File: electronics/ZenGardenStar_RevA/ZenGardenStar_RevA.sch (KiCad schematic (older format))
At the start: 20 parts, among them P1 CONN_01X02, P2 CONN_01X02, U1 A6211, U2 LM317_SOT223, U3 ArduinoProMini328, U4 MCP1700, U5 NRF24L01+

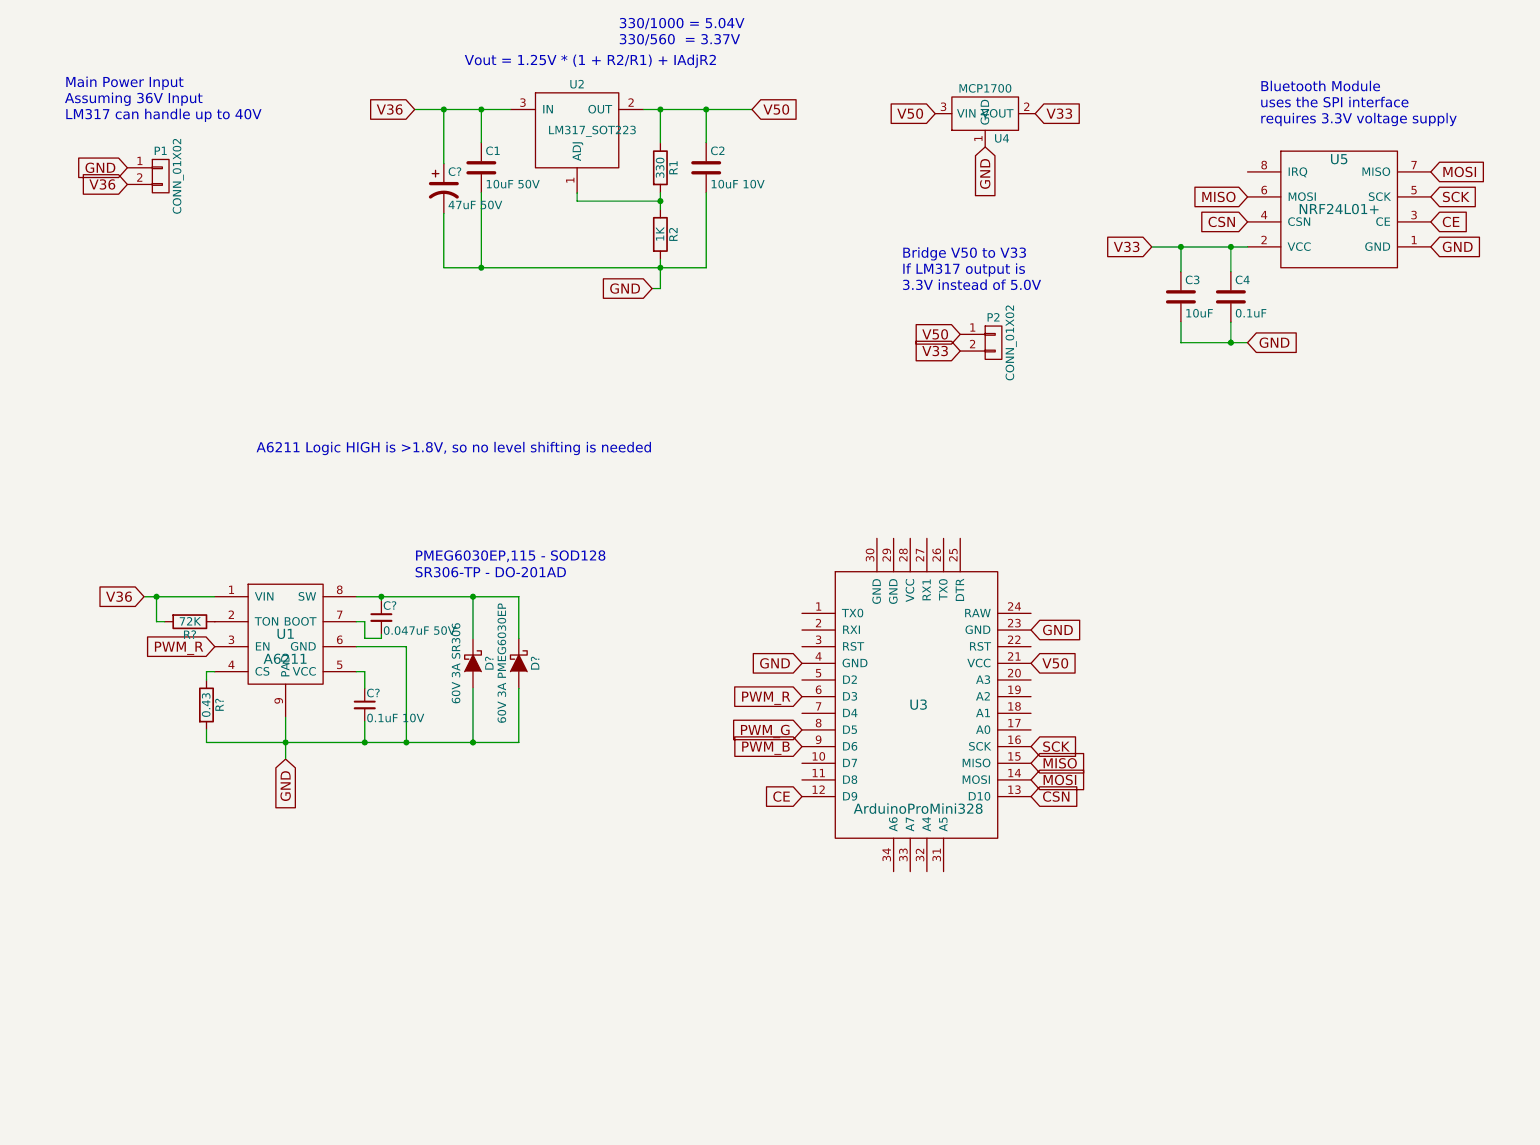
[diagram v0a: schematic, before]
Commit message: updated schematic for star
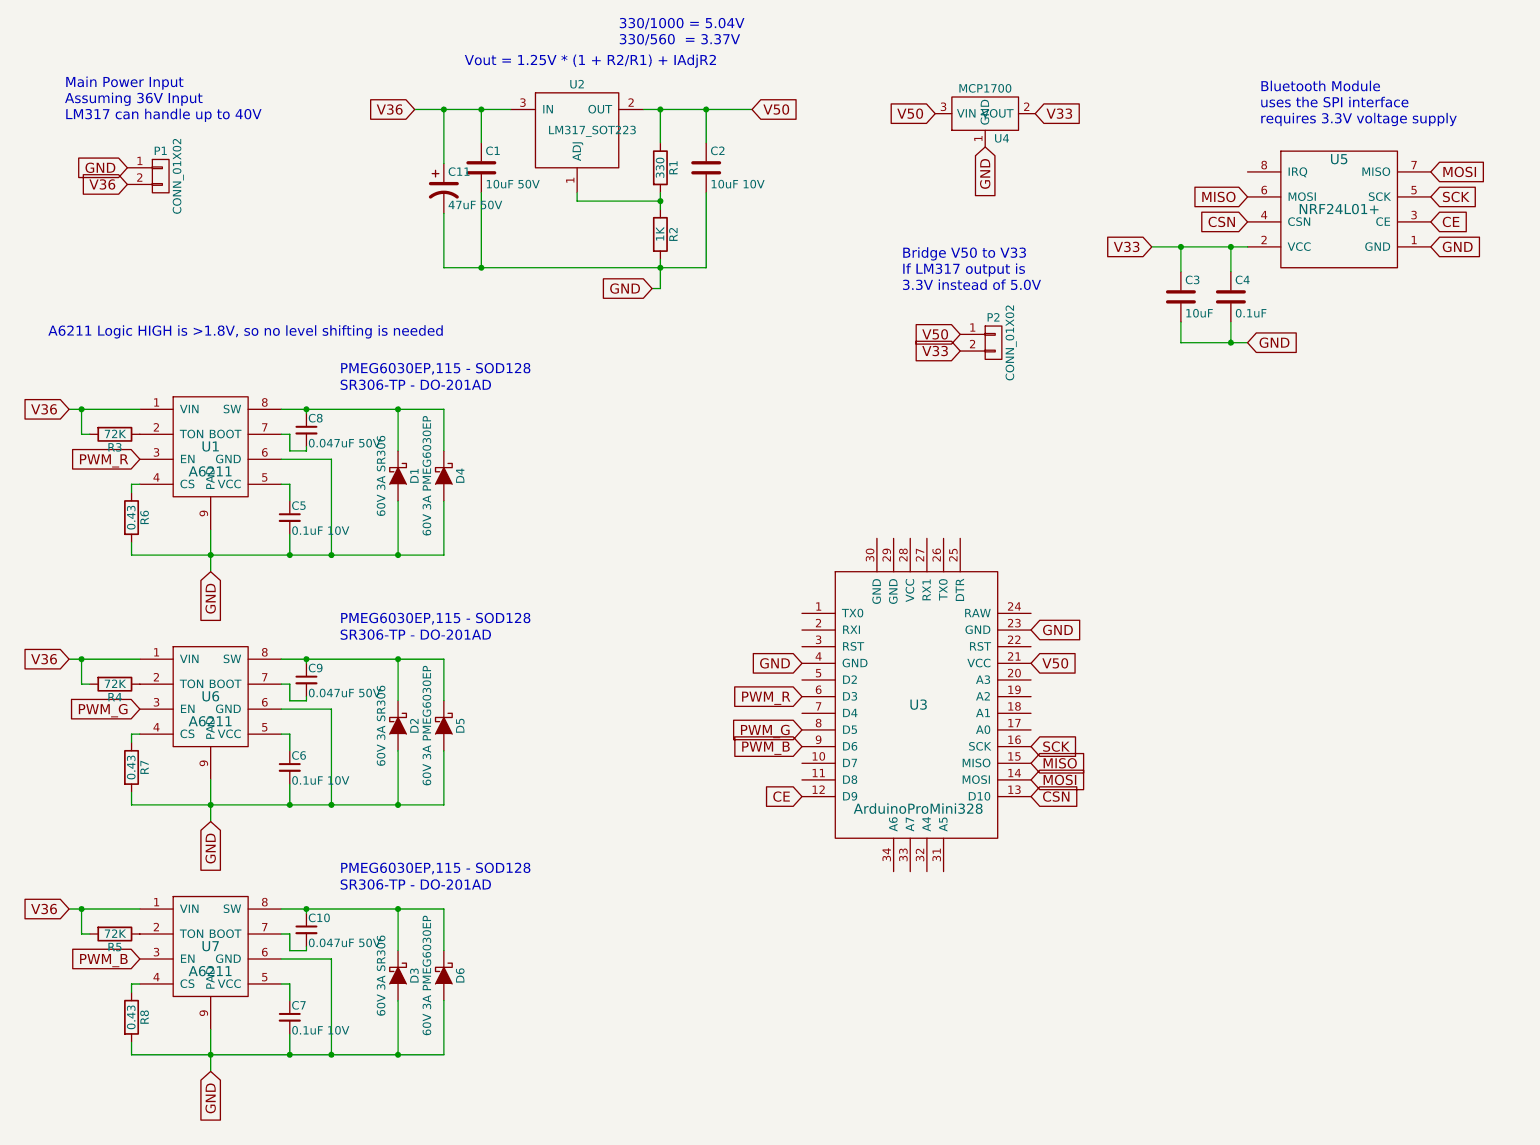
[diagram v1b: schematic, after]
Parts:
- added C10, C9: 0.047uF 50V, Capacitors_SMD:C_0805, symbol C_Small
- added C6, C7: 0.1uF 10V, Capacitors_SMD:C_0805, symbol C_Small
- added D2, D3: 60V 3A SR306, Diodes_ThroughHole:Diode_DO-201AD_Horizontal_RM15, symbol D_Schottky
- added D5, D6: 60V 3A PMEG6030EP, Diodes_SMD:SOD-123, symbol D_Schottky
- added R4, R5: 72K, Resistors_SMD:R_1206, symbol R
- added R7, R8: 0.43, Resistors_SMD:R_1206, symbol R
- added U6, U7: A6211, Housings_SOIC:SOIC-8-1EP_3.9x4.9mm_Pitch1.27mm, symbol A6211
- C11: renamed from C?; footprint (none) -> Capacitors_ThroughHole:C_Radial_D7.5_L11.2_P2.5
- C5, C8: renamed from C?; footprint (none) -> Capacitors_SMD:C_0805
- D1: renamed from D?; footprint (none) -> Diodes_ThroughHole:Diode_DO-201AD_Horizontal_RM15
- D4: renamed from D?; footprint (none) -> Diodes_SMD:SOD-123
- gave numbers to parts that had none: 2
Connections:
- net GND: now also C6.2, C7.2, D2.2 (A), D3.2 (A), D5.2 (A), D6.2 (A), R7.2, R8.2, U6.6 (GND), U6.9 (PAD), U7.6 (GND), U7.9 (PAD)
- net PWM_B: now also U7.3 (EN)
- net PWM_G: now also U6.3 (EN)
- net V36: now also R4.2, R5.2, U6.1 (VIN), U7.1 (VIN)
- new net: R4.1, U6.2 (TON)
- new net: R7.1, U6.4 (CS)
- new net: C6.1, U6.5 (VCC)
- new net: C9.2, U6.7 (BOOT)
- new net: C9.1, D2.1 (K), D5.1 (K), U6.8 (SW)
- new net: R5.1, U7.2 (TON)
- new net: R8.1, U7.4 (CS)
- new net: C7.1, U7.5 (VCC)
- new net: C10.2, U7.7 (BOOT)
- new net: C10.1, D3.1 (K), D6.1 (K), U7.8 (SW)
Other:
- moved on the sheet: C5, C8, D1, D4, R3, R6, U1

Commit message: updated star layout and schematic and render, at 80-90% done
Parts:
- added L1, L2, L3: INDUCTOR_SMALL, Inductors:SELF-WE-PD-XXL, symbol INDUCTOR_SMALL
- added P3: CONN_PIR_0, Pin_Headers:Pin_Header_Straight_1x03, symbol CONN_01X03
- added P4: CONN_PIR_1, Pin_Headers:Pin_Header_Straight_1x03, symbol CONN_01X03
- added P5: CONN_R, Pin_Headers:Pin_Header_Straight_1x02, symbol CONN_01X02
- added P6: CONN_B, Pin_Headers:Pin_Header_Straight_1x02, symbol CONN_01X02
- added P7: CONN_G, Pin_Headers:Pin_Header_Straight_1x02, symbol CONN_01X02
- P2: value CONN_01X02 -> CONN_VDD
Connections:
- net GND: now also P3.1 (P1), P4.1 (P1)
- net V50: now also P3.3 (P3), P4.3 (P3)
- net PIR_0: now reaches U3.10 (D7)
- net PIR_0: now also P3.2 (P2)
- net PIR_1: now reaches U3.11 (D8)
- net PIR_1: now also P4.2 (P2)
- net at R6.1, U1.4 (CS): now also P5.1 (P1)
- net at C8.1, D1.1 (K), D4.1 (K)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: now also L1.1
- net at R7.1, U6.4 (CS): now also P7.1 (P1)
- net at C9.1, D2.1 (K), D5.1 (K)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: now also L2.1
- net at R8.1, U7.4 (CS): now also P6.1 (P1)
- net at C10.1, D3.1 (K), D6.1 (K)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: now also L3.1
- new net: L1.2, P5.2 (P2)
- new net: L2.2, P7.2 (P2)
- new net: L3.2, P6.2 (P2)
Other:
- note added: "PIR Sensor 5-20V Input\n3.3V Digital Output"
- moved on the sheet: R6, R7, R8

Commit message: some updates to the star schematics and layout; schematic pretty much final
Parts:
- added C12: 100uF 50V, Capacitors_ThroughHole:C_Radial_D8_L13_P3.8, symbol CP1
- added P10: CONN_I2C, Pin_Headers:Pin_Header_Straight_1x04, symbol CONN_01X04
- added P8: CONN_A0, Pin_Headers:Pin_Header_Straight_1x03, symbol CONN_01X03
- added P9: CONN_A1, Pin_Headers:Pin_Header_Straight_1x03, symbol CONN_01X03
- L1, L2, L3: value INDUCTOR_SMALL -> 47uH 1A; footprint Inductors:SELF-WE-PD-XXL -> MyKiCadParts:TAIYO_YUDEN_IND_6045
- P1: footprint Terminal_Blocks:TerminalBlock_Pheonix_PT-3.5mm_2pol -> Connect:AK300-2
- P3, P4: footprint Pin_Headers:Pin_Header_Straight_1x03 -> Pin_Headers:Pin_Header_Angled_1x03
- P5, P6, P7: footprint Pin_Headers:Pin_Header_Straight_1x02 -> Connect:AK300-2
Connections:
- net GND: now also C12.2, P10.1 (P1), P8.1 (P1), P9.1 (P1)
- net V36: now also C12.1
- net V50: now also P10.2 (P2), P8.2 (P2), P9.2 (P2)
- net A0: now reaches U3.17 (A0)
- net A0: now also P8.3 (P3)
- net A1: now reaches U3.18 (A1)
- net A1: now also P9.3 (P3)
- net SCL: now reaches U3.31 (A5)
- net SCL: now also P10.4 (P4)
- net SDA: now reaches U3.32 (A4)
- net SDA: now also P10.3 (P3)
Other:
- note added: "Bluetooth Module\nuses the SPI interface\nrequires 3.3V voltage supply\npins are 5V tolerant though"
- note added: "PMEG6030EP,115 - SOD128 OR"
- note removed: "Bluetooth Module\nuses the SPI interface\nrequires 3.3V voltage supply"
- moved on the sheet: P3, P4, U3
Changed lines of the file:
@@
 Sheet 1 1
 Title "ZenGardenStar"
-Date "2017-03-09"
+Date "2017-03-11"
 Rev "A"
 Comp "D.O.P.E."
@@
 F 0 "P1" H 1925 2000 50  0000 C CNN
 F 1 "CONN_01X02" V 2025 1850 50  0000 C CNN
-F 2 "Terminal_Blocks:TerminalBlock_Pheonix_PT-3.5mm_2pol" H 1925 1850 50  0001 C CNN
+F 2 "Connect:AK300-2" H 1925 1850 50  0001 C CNN
 F 3 "" H 1925 1850 50  0000 C CNN
 	1    1925 1850
@@
 L ArduinoProMini328 U3
 U 1 1 58BB7402
-P 6475 5025
-F 0 "U3" H 6475 5025 60  0000 C CNN
-F 1 "ArduinoProMini328" H 6475 4400 60  0000 C CNN
-F 2 "MyKiCadParts:ArduinoProMini328" H 6475 5025 60  0001 C CNN
-F 3 "" H 6475 5025 60  0001 C CNN
-	1    6475 5025
+P 6550 4750
+F 0 "U3" H 6550 4750 60  0000 C CNN
+F 1 "ArduinoProMini328" H 6550 4125 60  0000 C CNN
+F 2 "MyKiCadParts:ArduinoProMini328" H 6550 4750 60  0001 C CNN
+F 3 "" H 6550 4750 60  0001 C CNN
+	1    6550 4750
 	1    0    0    -1
 $EndComp
 Text GLabel 7875 2275 0    60   Input ~ 0
 V33
-Text GLabel 7150 5275 2    60   Input ~ 0
+Text GLabel 7225 5000 2    60   Input ~ 0
 SCK
-Text GLabel 7150 5375 2    60   Input ~ 0
+Text GLabel 7225 5100 2    60   Input ~ 0
 MISO
-Text GLabel 7150 5475 2    60   Input ~ 0
+Text GLabel 7225 5200 2    60   Input ~ 0
 MOSI
-Text GLabel 7150 5575 2    60   Input ~ 0
+Text GLabel 7225 5300 2    60   Input ~ 0
 CSN
-Text GLabel 5775 5575 0    60   Input ~ 0
+Text GLabel 5850 5300 0    60   Input ~ 0
 CE
 Text GLabel 9550 2125 2    60   Input ~ 0
@@
 Text GLabel 9550 1825 2    60   Input ~ 0
 MOSI
-Text GLabel 7150 4575 2    60   Input ~ 0
+Text GLabel 7225 4300 2    60   Input ~ 0
 GND
 Text GLabel 9550 2275 2    60   Input ~ 0
@@
 GND
 Text Notes 8525 1550 0    60   ~ 0
-Bluetooth Module\nuses the SPI interface\nrequires 3.3V voltage supply
-Text GLabel 5775 4975 0    60   Input ~ 0
+Bluetooth Module\nuses the SPI interface\nrequires 3.3V voltage supply\npins are 5V tolerant though
+Text GLabel 5850 4700 0    60   Input ~ 0
 PWM_R
-Text GLabel 5775 5175 0    60   Input ~ 0
+Text GLabel 5850 4900 0    60   Input ~ 0
 PWM_G
-Text GLabel 5775 5275 0    60   Input ~ 0
+Text GLabel 5850 5000 0    60   Input ~ 0
 PWM_B
-Text GLabel 5775 4775 0    60   Input ~ 0
-GND
-Text GLabel 7150 4775 2    60   Input ~ 0
+Text GLabel 5850 4500 0    60   Input ~ 0
+GND
+Text GLabel 7225 4500 2    60   Input ~ 0
 V50
 Text GLabel 6575 1475 0    60   Input ~ 0
@@
 	1    0    0    -1
 $EndComp
-Text GLabel 3450 1450 0    60   Input ~ 0
+Text GLabel 3075 1450 0    60   Input ~ 0
 V36
 Text GLabel 4875 2525 0    60   Input ~ 0
@@
 $EndComp
 Text Notes 3000 3050 0    60   ~ 0
-PMEG6030EP,115 - SOD128
+PMEG6030EP,115 - SOD128   OR
 Text Notes 3000 3150 0    60   ~ 0
 SR306-TP - DO-201AD
@@
 L CONN_01X03 P3
 U 1 1 58C21485
-P 8550 4550
-F 0 "P3" H 8550 4750 50  0000 C CNN
-F 1 "CONN_PIR_0" V 8650 4550 50  0000 C CNN
-F 2 "Pin_Headers:Pin_Header_Straight_1x03" H 8550 4550 50  0001 C CNN
-F 3 "" H 8550 4550 50  0000 C CNN
-	1    8550 4550
-	1    0    0    -1
-$EndComp
-Text GLabel 8350 4650 0    60   Input ~ 0
+P 8950 4075
+F 0 "P3" H 8950 4275 50  0000 C CNN
+F 1 "CONN_PIR_0" V 9050 4075 50  0000 C CNN
+F 2 "Pin_Headers:Pin_Header_Angled_1x03" H 8950 4075 50  0001 C CNN
+F 3 "" H 8950 4075 50  0000 C CNN
+	1    8950 4075
+	1    0    0    -1
+$EndComp
+Text GLabel 8750 4175 0    60   Input ~ 0
 V50
-Text GLabel 8350 4450 0    60   Input ~ 0
-GND
-Text GLabel 8350 4550 0    60   Input ~ 0
+Text GLabel 8750 3975 0    60   Input ~ 0
+GND
+Text GLabel 8750 4075 0    60   Input ~ 0
 PIR_0
-Text GLabel 5775 5375 0    60   Input ~ 0
+Text GLabel 5850 5100 0    60   Input ~ 0
 PIR_0
-Text GLabel 5775 5475 0    60   Input ~ 0
+Text GLabel 5850 5200 0    60   Input ~ 0
 PIR_1
 $Comp
 L CONN_01X03 P4
 U 1 1 58C22968
-P 8550 5125
-F 0 "P4" H 8550 5325 50  0000 C CNN
-F 1 "CONN_PIR_1" V 8650 5125 50  0000 C CNN
-F 2 "Pin_Headers:Pin_Header_Straight_1x03" H 8550 5125 50  0001 C CNN
-F 3 "" H 8550 5125 50  0000 C CNN
-	1    8550 5125
-	1    0    0    -1
-$EndComp
-Text GLabel 8350 5225 0    60   Input ~ 0
+P 8950 4650
+F 0 "P4" H 8950 4850 50  0000 C CNN
+F 1 "CONN_PIR_1" V 9050 4650 50  0000 C CNN
+F 2 "Pin_Headers:Pin_Header_Angled_1x03" H 8950 4650 50  0001 C CNN
+F 3 "" H 8950 4650 50  0000 C CNN
+	1    8950 4650
+	1    0    0    -1
+$EndComp
+Text GLabel 8750 4750 0    60   Input ~ 0
 V50
-Text GLabel 8350 5025 0    60   Input ~ 0
-GND
-Text GLabel 8350 5125 0    60   Input ~ 0
+Text GLabel 8750 4550 0    60   Input ~ 0
+GND
+Text GLabel 8750 4650 0    60   Input ~ 0
 PIR_1
-Text Notes 7925 4200 0    60   ~ 0
+Text Notes 8325 3725 0    60   ~ 0
 PIR Sensor 5-20V Input\n3.3V Digital Output
 $Comp
@@
 F 0 "P7" H 4525 5150 50  0000 C CNN
 F 1 "CONN_G" V 4625 5000 50  0000 C CNN
-F 2 "Pin_Headers:Pin_Header_Straight_1x02" H 4525 5000 50  0001 C CNN
+F 2 "Connect:AK300-2" H 4525 5000 50  0001 C CNN
 F 3 "" H 4525 5000 50  0000 C CNN
 	1    4525 5000
@@
 F 0 "P6" H 4500 6650 50  0000 C CNN
 F 1 "CONN_B" V 4600 6500 50  0000 C CNN
-F 2 "Pin_Headers:Pin_Header_Straight_1x02" H 4500 6500 50  0001 C CNN
+F 2 "Connect:AK300-2" H 4500 6500 50  0001 C CNN
 F 3 "" H 4500 6500 50  0000 C CNN
 	1    4500 6500
@@
 P 3925 3250
 F 0 "L1" H 3925 3350 50  0000 C CNN
-F 1 "INDUCTOR_SMALL" H 3925 3200 50  0000 C CNN
-F 2 "Inductors:SELF-WE-PD-XXL" H 3925 3250 50  0001 C CNN
+F 1 "47uH 1A" H 3925 3200 50  0000 C CNN
+F 2 "MyKiCadParts:TAIYO_YUDEN_IND_6045" H 3925 3250 50  0001 C CNN
 F 3 "" H 3925 3250 50  0000 C CNN
 	1    3925 3250
@@
 P 3925 4750
 F 0 "L2" H 3925 4850 50  0000 C CNN
-F 1 "INDUCTOR_SMALL" H 3925 4700 50  0000 C CNN
-F 2 "Inductors:SELF-WE-PD-XXL" H 3925 4750 50  0001 C CNN
+F 1 "47uH 1A" H 3925 4700 50  0000 C CNN
+F 2 "MyKiCadParts:TAIYO_YUDEN_IND_6045" H 3925 4750 50  0001 C CNN
 F 3 "" H 3925 4750 50  0000 C CNN
 	1    3925 4750
@@
 P 3925 6250
 F 0 "L3" H 3925 6350 50  0000 C CNN
-F 1 "INDUCTOR_SMALL" H 3925 6200 50  0000 C CNN
-F 2 "Inductors:SELF-WE-PD-XXL" H 3925 6250 50  0001 C CNN
+F 1 "47uH 1A" H 3925 6200 50  0000 C CNN
+F 2 "MyKiCadParts:TAIYO_YUDEN_IND_6045" H 3925 6250 50  0001 C CNN
 F 3 "" H 3925 6250 50  0000 C CNN
 	1    3925 6250
@@
 	4925 2350 4925 2525
 Wire Wire Line
-	3450 1450 4025 1450
+	3075 1450 4025 1450
 Wire Wire Line
 	4825 1450 5475 1450
@@
 	5200 2400 5200 1950
 Wire Wire Line
-	3625 2400 5200 2400
+	3325 2400 5200 2400
 Wire Wire Line
 	3850 2400 3850 1950
@@
 F 0 "P5" H 4475 3650 50  0000 C CNN
 F 1 "CONN_R" V 4575 3500 50  0000 C CNN
-F 2 "Pin_Headers:Pin_Header_Straight_1x02" H 4475 3500 50  0001 C CNN
+F 2 "Connect:AK300-2" H 4475 3500 50  0001 C CNN
 F 3 "" H 4475 3500 50  0000 C CNN
 	1    4475 3500
@@
 	3950 5250 3950 5050
 Connection ~ 4225 5050
+$Comp
+L CP1 C12
+U 1 1 58C46F27
+P 3325 2075
+F 0 "C12" H 3350 2175 50  0000 L CNN
+F 1 "100uF 50V" H 3350 1975 50  0000 L CNN
+F 2 "Capacitors_ThroughHole:C_Radial_D8_L13_P3.8" H 3325 2075 50  0001 C CNN
+F 3 "" H 3325 2075 50  0000 C CNN
+	1    3325 2075
+	1    0    0    -1
+$EndComp
+Wire Wire Line
+	3325 1925 3325 1450
+Connection ~ 3325 1450
+Wire Wire Line
+	3325 2225 3325 2400
+Connection ~ 3625 2400
+$Comp
+L CONN_01X03 P8
+U 1 1 58C4CE75
+P 8975 5225
+F 0 "P8" H 8975 5425 50  0000 C CNN
+F 1 "CONN_A0" V 9075 5225 50  0000 C CNN
+F 2 "Pin_Headers:Pin_Header_Straight_1x03" H 8975 5225 50  0001 C CNN
+F 3 "" H 8975 5225 50  0000 C CNN
+	1    8975 5225
+	1    0    0    -1
+$EndComp
+Text GLabel 8775 5125 0    60   Input ~ 0
+GND
+Text GLabel 8775 5225 0    60   Input ~ 0
+V50
+Text GLabel 8775 5325 0    60   Input ~ 0
+A0
+Text GLabel 7225 4900 2    60   Input ~ 0
+A0
+Text GLabel 7225 4800 2    60   Input ~ 0
+A1
+$Comp
+L CONN_01X03 P9
+U 1 1 58C4E897
+P 8975 5650
+F 0 "P9" H 8975 5850 50  0000 C CNN
+F 1 "CONN_A1" V 9075 5650 50  0000 C CNN
+F 2 "Pin_Headers:Pin_Header_Straight_1x03" H 8975 5650 50  0001 C CNN
+F 3 "" H 8975 5650 50  0000 C CNN
+	1    8975 5650
+	1    0    0    -1
+$EndComp
+Text GLabel 8775 5550 0    60   Input ~ 0
+GND
+Text GLabel 8775 5750 0    60   Input ~ 0
+A1
+Text GLabel 8775 5650 0    60   Input ~ 0
+V50
+$Comp
+L CONN_01X04 P10
+U 1 1 58C51FAA
+P 9825 5625
+F 0 "P10" H 9825 5875 50  0000 C CNN
+F 1 "CONN_I2C" V 9925 5625 50  0000 C CNN
+F 2 "Pin_Headers:Pin_Header_Straight_1x04" H 9825 5625 50  0001 C CNN
+F 3 "" H 9825 5625 50  0000 C CNN
+	1    9825 5625
+	1    0    0    -1
+$EndComp
+Text GLabel 9625 5475 0    60   Input ~ 0
+GND
+Text GLabel 9625 5575 0    60   Input ~ 0
+V50
+Text GLabel 9625 5675 0    60   Input ~ 0
+SDA
+Text GLabel 9625 5775 0    60   Input ~ 0
+SCL
+Text GLabel 6600 5750 3    60   Input ~ 0
+SDA
+Text GLabel 6700 5750 3    60   Input ~ 0
+SCL
 $EndSCHEMATC

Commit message: near final pcb layout
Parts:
- P3, P4: footprint Pin_Headers:Pin_Header_Angled_1x03 -> Pin_Headers:Pin_Header_Straight_1x03
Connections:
- net PIR_0: now also U3.19 (A2); no longer U3.10 (D7)
- net PIR_1: now also U3.20 (A3); no longer U3.11 (D8)
- net at R6.1, U1.4 (CS): now also P5.2 (P2); no longer P5.1 (P1)
- net at R7.1, U6.4 (CS): now also P7.2 (P2); no longer P7.1 (P1)
- net at R8.1, U7.4 (CS): now also P6.2 (P2); no longer P6.1 (P1)
- net at L1.2: now also P5.1 (P1); no longer P5.2 (P2)
- net at L2.2: now also P7.1 (P1); no longer P7.2 (P2)
- net at L3.2: now also P6.1 (P1); no longer P6.2 (P2)
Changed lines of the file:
@@
 F 0 "P3" H 8950 4275 50  0000 C CNN
 F 1 "CONN_PIR_0" V 9050 4075 50  0000 C CNN
-F 2 "Pin_Headers:Pin_Header_Angled_1x03" H 8950 4075 50  0001 C CNN
+F 2 "Pin_Headers:Pin_Header_Straight_1x03" H 8950 4075 50  0001 C CNN
 F 3 "" H 8950 4075 50  0000 C CNN
 	1    8950 4075
@@
 Text GLabel 8750 4075 0    60   Input ~ 0
 PIR_0
-Text GLabel 5850 5100 0    60   Input ~ 0
+Text GLabel 7225 4700 2    60   Input ~ 0
 PIR_0
-Text GLabel 5850 5200 0    60   Input ~ 0
+Text GLabel 7225 4600 2    60   Input ~ 0
 PIR_1
 $Comp
@@
 F 0 "P4" H 8950 4850 50  0000 C CNN
 F 1 "CONN_PIR_1" V 9050 4650 50  0000 C CNN
-F 2 "Pin_Headers:Pin_Header_Angled_1x03" H 8950 4650 50  0001 C CNN
+F 2 "Pin_Headers:Pin_Header_Straight_1x03" H 8950 4650 50  0001 C CNN
 F 3 "" H 8950 4650 50  0000 C CNN
 	1    8950 4650
@@
 F 3 "" H 4525 5000 50  0000 C CNN
 	1    4525 5000
-	1    0    0    1
+	1    0    0    -1
 $EndComp
 $Comp
@@
 F 3 "" H 4500 6500 50  0000 C CNN
 	1    4500 6500
-	1    0    0    1
+	1    0    0    -1
 $EndComp
 $Comp
@@
 F 3 "" H 4475 3500 50  0000 C CNN
 	1    4475 3500
-	1    0    0    1
-$EndComp
-Wire Wire Line
+	1    0    0    -1
+$EndComp
+Wire Wire Line
